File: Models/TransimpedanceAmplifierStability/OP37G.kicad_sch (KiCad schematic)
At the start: 33 parts

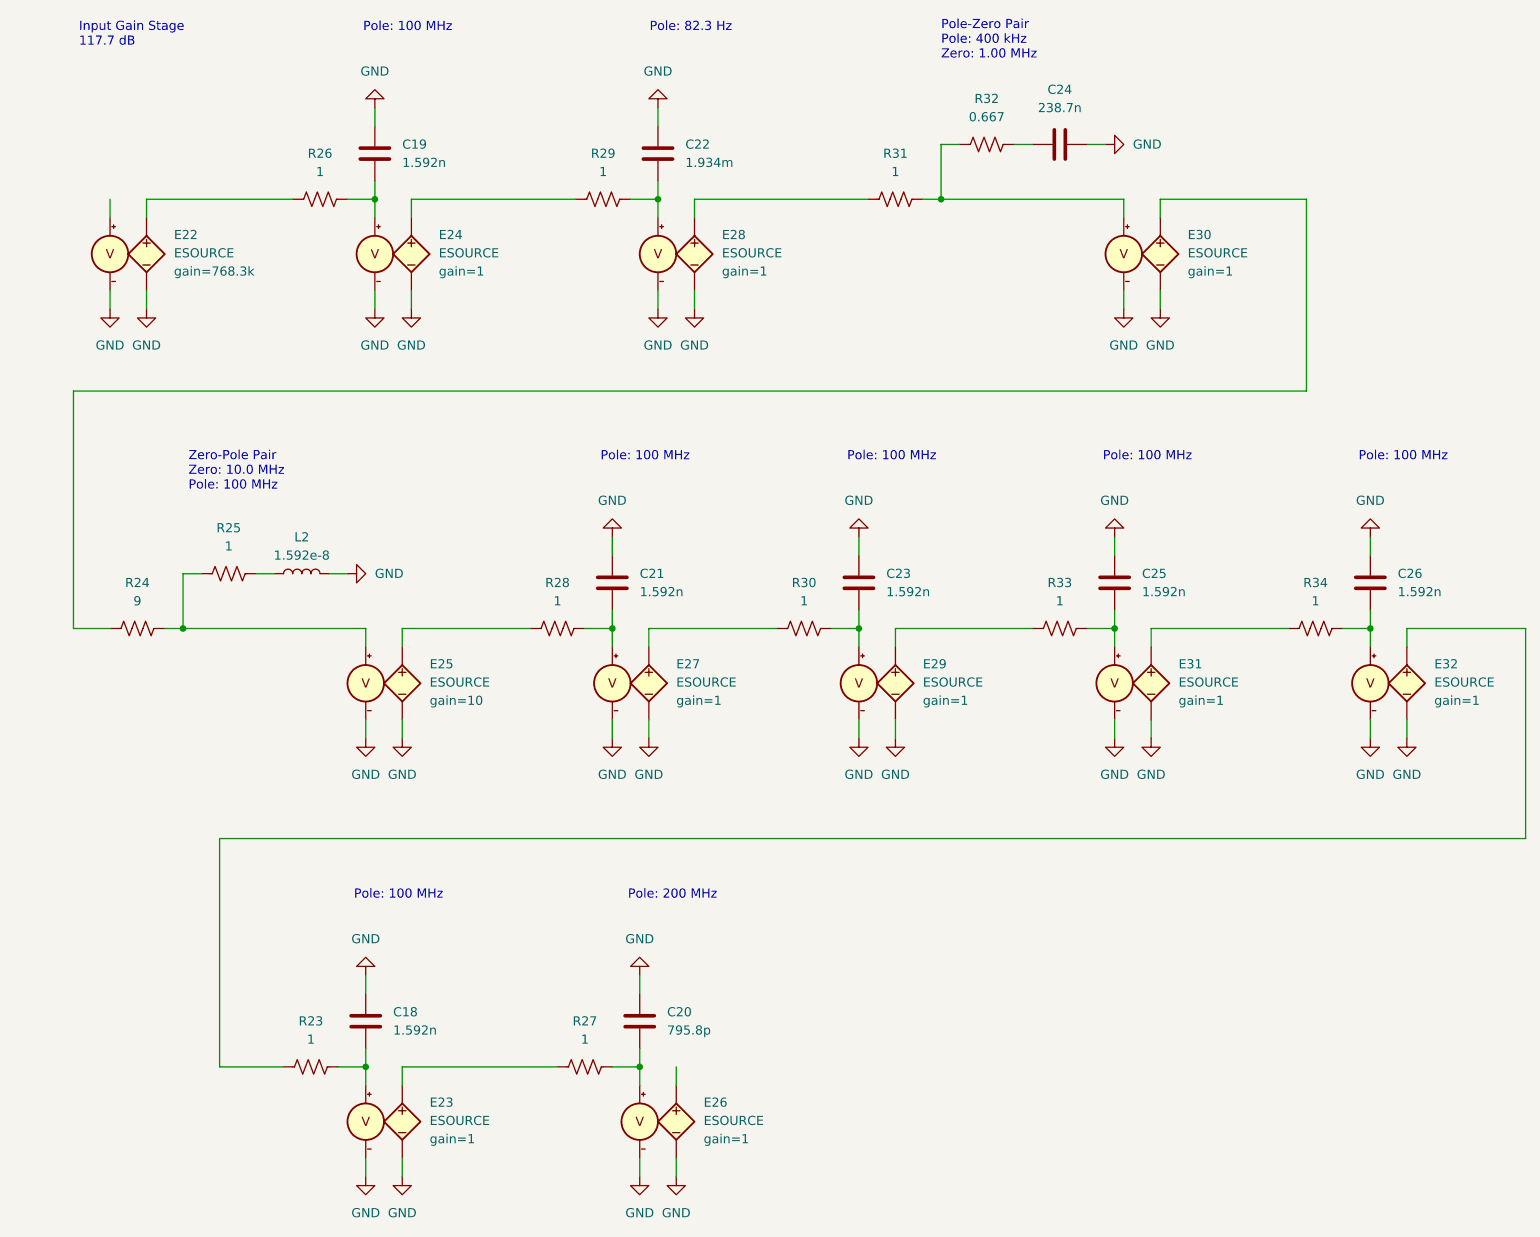
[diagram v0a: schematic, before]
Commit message: Upload latest version of TIA stability KiCad project
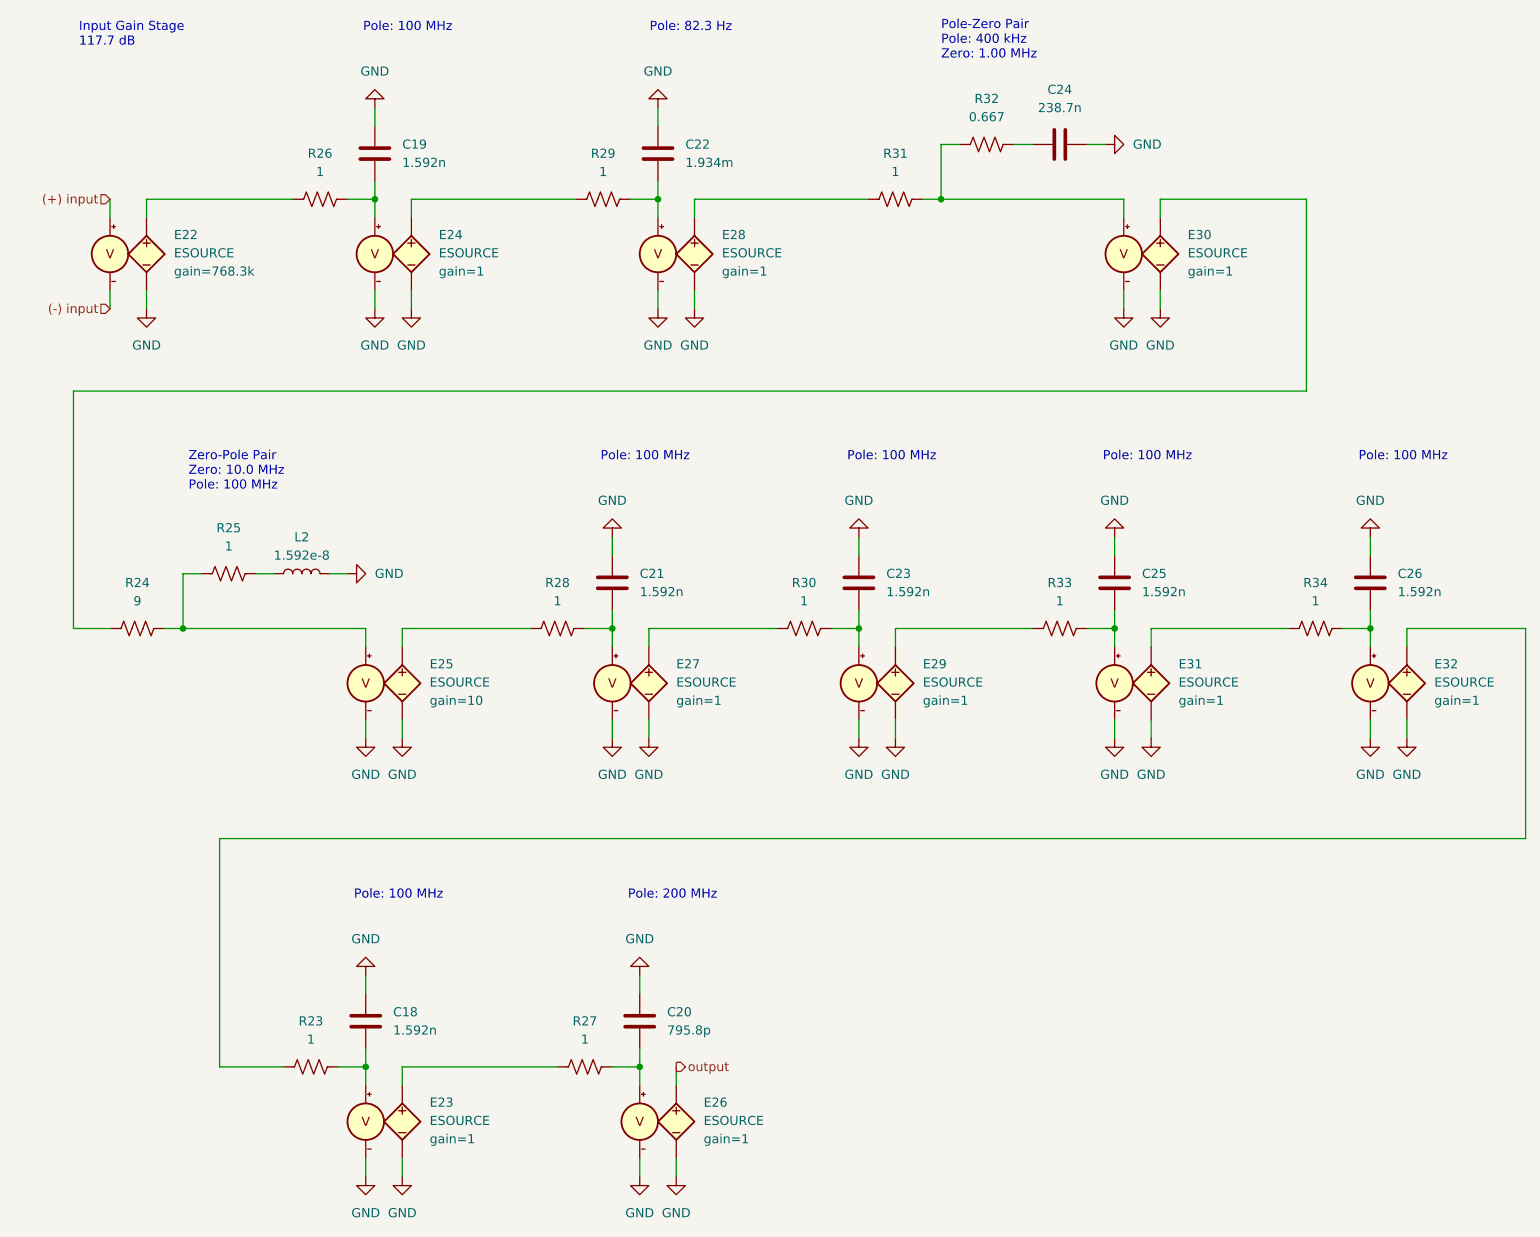
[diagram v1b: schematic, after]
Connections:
- net GND: no longer E22.4 (C-)
- net (+) input: now reaches E22.3 (C+)
- net output: now reaches E26.1 (N+)
- new net (-) input: E22.4 (C-)
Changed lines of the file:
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@@
 		)
 	)
+	(hierarchical_label "(+) input"
+		(shape input)
+		(at 59.69 44.45 180)
+		(effects
+			(font
+				(size 1.27 1.27)
+			)
+			(justify right)
+		)
+	)
+	(hierarchical_label "(-) input"
+		(shape input)
+		(at 59.69 59.69 180)
+		(effects
+			(font
+				(size 1.27 1.27)
+			)
+			(justify right)
+		)
+	)
+	(hierarchical_label "output"
+		(shape output)
+		(at 138.43 165.1 0)
+		(effects
+			(font
+				(size 1.27 1.27)
+			)
+			(justify left)
+		)
+	)
 	(symbol
 		(lib_id "power:GND")
@@
 					(unit 1)
 				)
-			)
-		)
-	)
-	(symbol
-		(lib_id "power:GND")
-		(at 59.69 59.69 0)
-		(unit 1)
-		(exclude_from_sim no)
-		(in_bom yes)
-		(on_board yes)
-		(dnp no)
-		(fields_autoplaced yes)
-		(property "Reference" "#PWR057"
-			(at 59.69 66.04 0)
-			(effects
-				(font
-					(size 1.27 1.27)
-				)
-				(hide yes)
-			)
-		)
-		(property "Value" "GND"
-			(at 59.69 64.77 0)
-			(effects
-				(font
-					(size 1.27 1.27)
-				)
-			)
-		)
-		(property "Footprint" ""
-			(at 59.69 59.69 0)
-			(effects
-				(font
-					(size 1.27 1.27)
-				)
-				(hide yes)
-			)
-		)
-		(property "Datasheet" ""
-			(at 59.69 59.69 0)
-			(effects
-				(font
-					(size 1.27 1.27)
-				)
-				(hide yes)
-			)
-		)
-		(property "Description" "Power symbol creates a global label with name \"GND\" , ground"
-			(at 59.69 59.69 0)
-			(effects
-				(font
-					(size 1.27 1.27)
-				)
-				(hide yes)
-			)
-		)
-		(pin "1"
-		)
-		(instances
-			(project "TransimpedanceAmplifierStability"
-				(path "/b282eeea-1083-4bd9-aef5-c78f2e129a69/c37de297-4abe-44bd-aa0f-b4ce0cdbfb93"
-					(reference "#PWR057")
-					(unit 1)
-				)
